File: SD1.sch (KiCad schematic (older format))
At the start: 46 parts, among them J103 JST ZH 1.5mm 1x5, J104 JST 1.25mm, J107 JST 1.25mm, Q101 BSS138, Q102 PDTC114EU,115, SW103 Multidirection_Switch, U102 ER-TFTM028-4, U104 CC2652P, U106 EKMC1691111, U107 MCP23017, U108 BME280, U109 SCD30

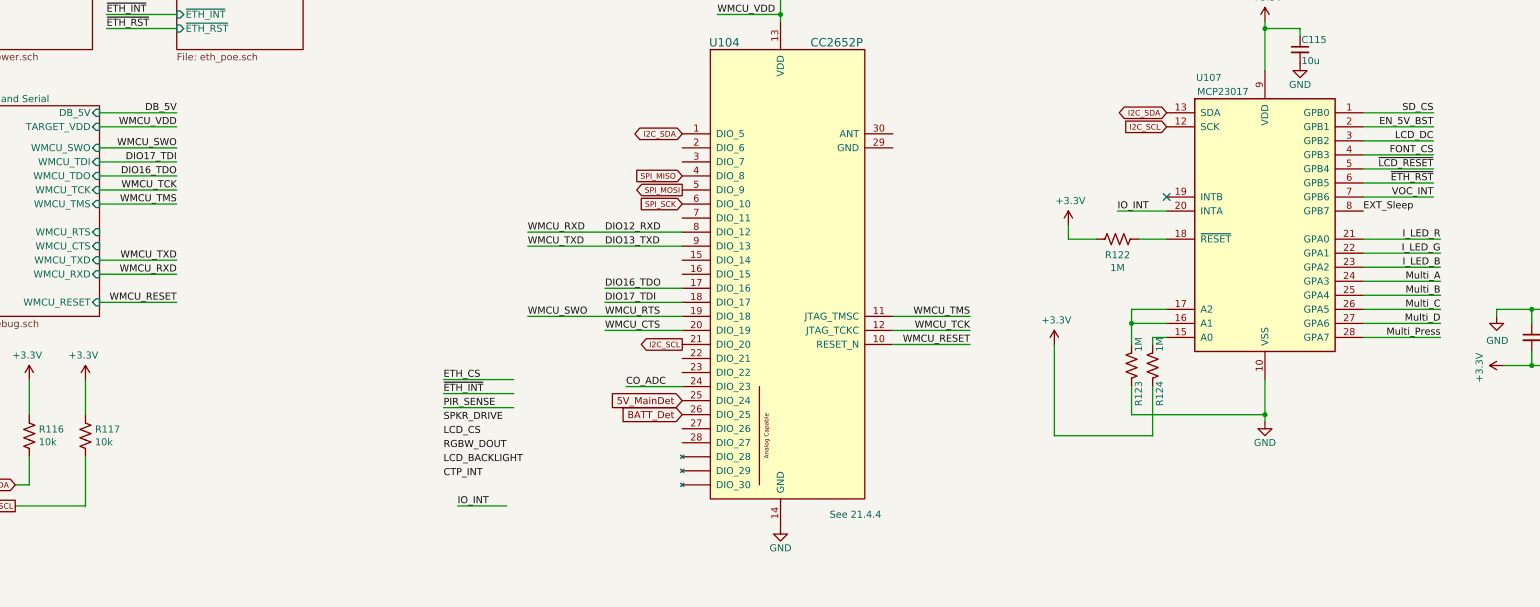
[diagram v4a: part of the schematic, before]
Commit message: 4layer layout WIP, 90%.
Changed SCD30 to reverse mount. 
Connected RGB led and button to io expander.
Connected all nets to micro.
Add jumper for CTS line.
Nettie GNDA and GND for W5500 Eth.
Changed EN_5V_BST to Global.
Bugfixes net names: LCD_CS
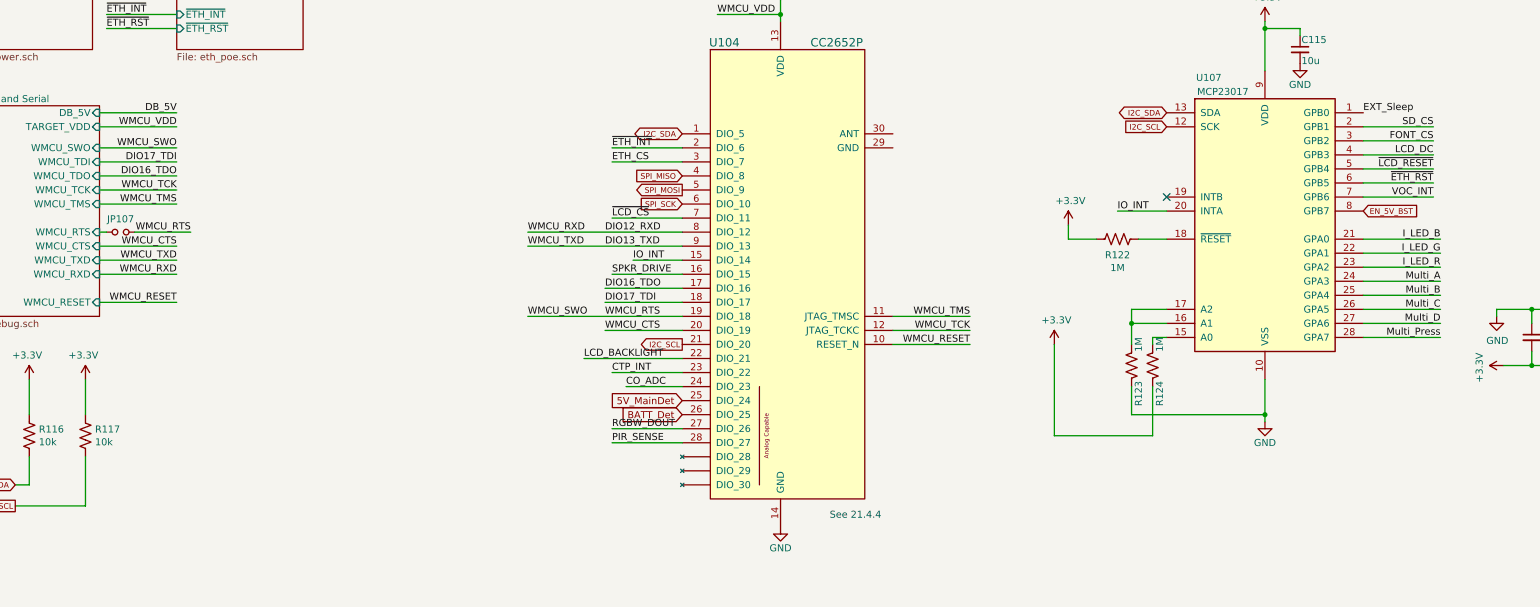
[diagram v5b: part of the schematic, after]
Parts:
- added JP107: Jumper_NO_Small, Jumper:SolderJumper-2_P1.3mm_Open_RoundedPad1.0x1.5mm, symbol Device:Jumper_NO_Small
- U109: footprint mylib:SCD30 -> mylib:SCD30_reverse_mount
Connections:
- net CTP_INT: now also U104.23 (DIO_22)
- net Debug and Serial/WMCU_RTS: now also JP107.1
- net EN_5V_BST: now also U107.8 (GPB7); no longer U107.2 (GPB1)
- net ETH_CS: now also U104.3 (DIO_7)
- net EXT_Sleep: now also U107.1 (GPB0); no longer U107.8 (GPB7)
- net FONT_CS: now also U107.3 (GPB2); no longer U107.4 (GPB3)
- net IO_INT: now also U104.15 (DIO_14)
- net I_LED_B: now also U107.21 (GPA0); no longer U107.23 (GPA2)
- net I_LED_R: now also U107.23 (GPA2); no longer U107.21 (GPA0)
- net LCD_BACKLIGHT: now also U104.22 (DIO_21)
- net LCD_DC: now also U107.4 (GPB3); no longer U107.3 (GPB2)
- net PIR_SENSE: now also U104.28 (DIO_27)
- net RGBW_DOUT: now also U104.27 (DIO_26)
- net SD_CS: now also U107.2 (GPB1); no longer U107.1 (GPB0)
- net SPKR_DRIVE: now also U104.16 (DIO_15)
- net WMCU_RTS: now also JP107.2
- net ~ETH_INT: now also U104.2 (DIO_6)
- net ~LCD_CS: now also U104.7 (DIO_11)
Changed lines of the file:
@@
 Text GLabel 13850 1700 2    40   Output ~ 0
 SPI_MISO
-Text Label 11150 1750 2    50   ~ 0
+Text Label 11150 1850 2    50   ~ 0
 SD_CS
-Text Label 11150 2050 2    50   ~ 0
+Text Label 11150 1950 2    50   ~ 0
 FONT_CS
 Text Label 14050 1050 2    50   ~ 0
 ~LCD_CS
-Text Label 4100 4050 0    50   ~ 0
-LCD_CS
 Text Label 14050 900  2    50   ~ 0
 ~LCD_RESET
@@
 Text Label 14050 1250 2    50   ~ 0
 LCD_DC
-Text Label 11150 1950 2    50   ~ 0
+Text Label 11150 2050 2    50   ~ 0
 LCD_DC
-Text Label 4100 4250 0    50   ~ 0
+Text Label 5100 3500 0    50   ~ 0
 LCD_BACKLIGHT
 Wire Wire Line
@@
 F 0 "U109" H 6097 7671 50  0000 R CNN
 F 1 "SCD30" H 6097 7580 50  0000 R CNN
-F 2 "mylib:SCD30" V 6400 7650 50  0001 C CNN
+F 2 "mylib:SCD30_reverse_mount" V 6400 7650 50  0001 C CNN
 F 3 "https://www.sensirion.com/fileadmin/user_upload/customers/sensirion/Dokumente/9.5_CO2/Sensirion_CO2_Sensors_SCD30_Datasheet.pdf" V 6675 7825 50  0001 C CNN
 F 4 "SCD30" H 6400 7650 50  0001 C CNN "MPN"
@@
 Text GLabel 5800 3800 0    50   Input ~ 0
 5V_MainDet
-Wire Wire Line
-	11150 1850 10650 1850
-Text Label 11150 1850 2    50   ~ 0
-EN_5V_BST
 Text Notes 3700 8800 0    50   ~ 0
 Particulates
@@
 CO_ADC
 Wire Wire Line
-	4100 3850 4600 3850
-Text Label 4100 3850 0    50   ~ 0
+	5300 4100 5800 4100
+Text Label 5300 4100 0    50   ~ 0
 PIR_SENSE
-Text Label 4100 4350 0    50   ~ 0
+Text Label 5300 3600 0    50   ~ 0
 CTP_INT
 Wire Wire Line
@@
 Text Label 11150 2250 2    50   ~ 0
 ~ETH_RST
-Wire Wire Line
-	4100 3750 4600 3750
-Text Label 4100 3750 0    50   ~ 0
-~ETH_INT
-Wire Wire Line
-	4100 3650 4600 3650
-Text Label 4100 3650 0    50   ~ 0
-ETH_CS
-Text Label 4200 4550 0    50   ~ 0
+Text Label 5450 2800 0    50   ~ 0
 IO_INT
 Wire Wire Line
-	4200 4550 4550 4550
+	5450 2800 5800 2800
 Wire Wire Line
 	11150 2350 10650 2350
 Text Label 11150 2350 2    50   ~ 0
 VOC_INT
-Wire Wire Line
-	10650 2650 11200 2650
-Wire Wire Line
-	10650 2750 11200 2750
-Wire Wire Line
-	10650 2850 11200 2850
-Text Label 11200 2650 2    50   ~ 0
-I_LED_R
-Text Label 11200 2750 2    50   ~ 0
-I_LED_G
-Text Label 11200 2850 2    50   ~ 0
-I_LED_B
 NoConn ~ 8550 10150
 Wire Wire Line
@@
 Text Label 8100 9750 0    50   ~ 0
 EXT_Sleep
-Text Label 10650 2450 0    50   ~ 0
+Text Label 10650 1750 0    50   ~ 0
 EXT_Sleep
 Wire Wire Line
@@
 Text Label 11200 3350 2    50   ~ 0
 Multi_Press
-Text Label 4100 3950 0    50   ~ 0
+Text Label 5300 2900 0    50   ~ 0
 SPKR_DRIVE
 Wire Wire Line
 	11150 2150 10650 2150
 Wire Wire Line
-	11150 2050 10650 2050
-Wire Wire Line
 	11150 1950 10650 1950
 $Comp
@@
 $EndComp
 Wire Wire Line
-	11150 1750 10650 1750
+	11150 1850 10650 1850
 Text GLabel 5800 3900 0    50   Input ~ 0
 BATT_Det
@@
 Text Label 14500 7200 0    50   ~ 0
 RGBW_DOUT
-Text Label 4100 4150 0    50   ~ 0
+Text Label 5300 4000 0    50   ~ 0
 RGBW_DOUT
+Text Label 11200 2650 2    50   ~ 0
+I_LED_B
+Text Label 11200 2750 2    50   ~ 0
+I_LED_G
+Text Label 11200 2850 2    50   ~ 0
+I_LED_R
+Wire Wire Line
+	10650 2650 11200 2650
+Wire Wire Line
+	10650 2750 11200 2750
+Wire Wire Line
+	10650 2850 11200 2850
+Wire Wire Line
+	2200 2700 1650 2700
+Text Label 2200 2700 2    50   ~ 0
+WMCU_CTS
+Wire Wire Line
+	1650 2600 1700 2600
+$Comp
+L Device:Jumper_NO_Small JP107
+U 1 1 5FFF492F
+P 1800 2600
+F 0 "JP107" H 1800 2693 50  0000 C CNN
+F 1 "Jumper_NO_Small" H 1800 2694 50  0001 C CNN
+F 2 "Jumper:SolderJumper-2_P1.3mm_Open_RoundedPad1.0x1.5mm" H 1800 2600 50  0001 C CNN
+F 3 "~" H 1800 2600 50  0001 C CNN
+	1    1800 2600
+	1    0    0    -1
+$EndComp
+Text Label 2300 2600 2    50   ~ 0
+WMCU_RTS
+Wire Wire Line
+	2300 2600 1900 2600
+Text GLabel 10650 2450 2    40   Input ~ 0
+EN_5V_BST
+Wire Wire Line
+	10650 2050 11150 2050
+Text Label 5300 2100 0    50   ~ 0
+ETH_CS
+Wire Wire Line
+	5300 2100 5800 2100
+Text Label 5300 2000 0    50   ~ 0
+~ETH_INT
+Wire Wire Line
+	5300 2000 5800 2000
+Wire Wire Line
+	5300 2900 5800 2900
+Wire Wire Line
+	5300 2500 5800 2500
+Text Label 5300 2500 0    50   ~ 0
+~LCD_CS
+Wire Wire Line
+	5300 3600 5800 3600
+Wire Wire Line
+	5300 4000 5800 4000
+Wire Wire Line
+	5100 3500 5800 3500
 $EndSCHEMATC

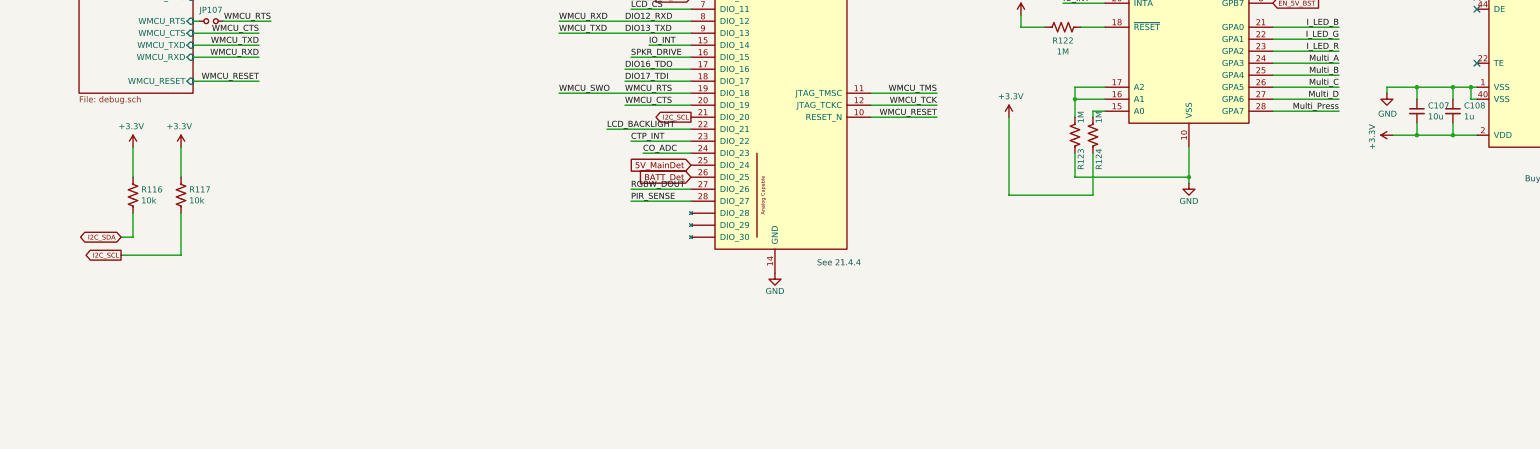
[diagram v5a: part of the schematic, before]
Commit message: Layout WIP, sch final
USB 5V Jumper works for both FTDI and microusb
Added decoupling caps for micro
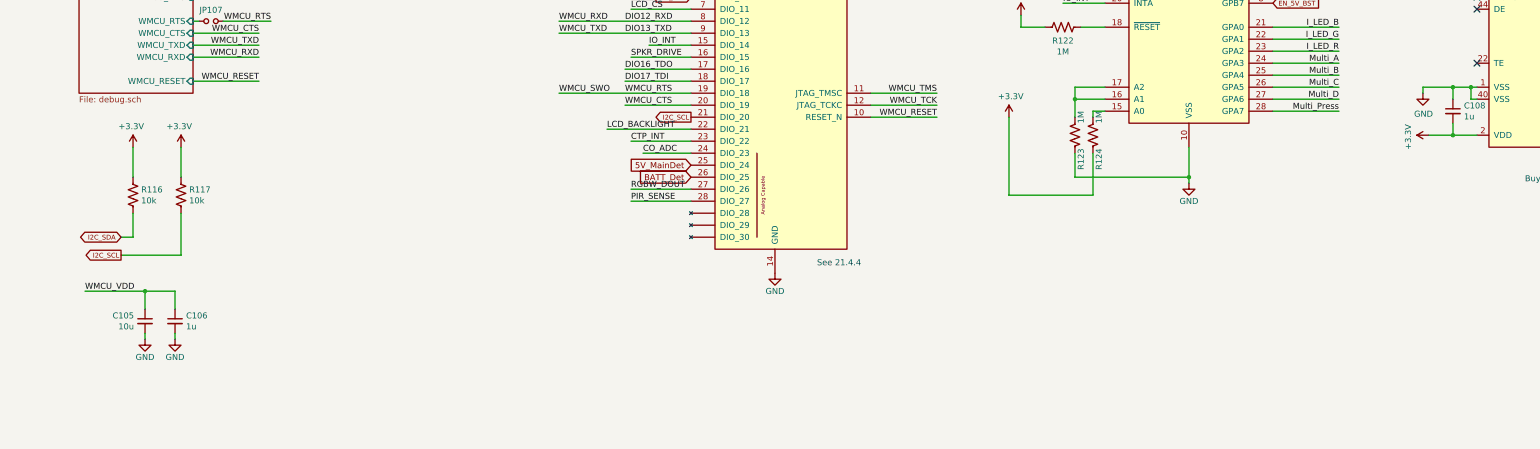
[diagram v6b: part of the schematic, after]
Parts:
- removed C107: 10u, Capacitor_SMD:C_1206_3216Metric, symbol Device:C_Small
- added C105: 10u, Capacitor_SMD:C_0603_1608Metric, symbol Device:C_Small
- added C106: 1u, Capacitor_SMD:C_0603_1608Metric, symbol Device:C_Small
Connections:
- net +3V3: now also C105.1, C106.1
- net GND: now also C105.2, C106.2
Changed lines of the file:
@@
 L power:+3.3V #PWR?
 U 1 1 5FA62239
-P 11650 3550
+P 11950 3550
 AR Path="/5E715318/5FA62239" Ref="#PWR?"  Part="1"
 AR Path="/5FA62239" Ref="#PWR0117"  Part="1"
-F 0 "#PWR0117" H 11650 3400 50  0001 C CNN
-F 1 "+3.3V" H 11665 3723 50  0000 C CNN
-F 2 "" H 11650 3550 50  0001 C CNN
-F 3 "" H 11650 3550 50  0001 C CNN
-	1    11650 3550
+F 0 "#PWR0117" H 11950 3400 50  0001 C CNN
+F 1 "+3.3V" H 11965 3723 50  0000 C CNN
+F 2 "" H 11950 3550 50  0001 C CNN
+F 3 "" H 11950 3550 50  0001 C CNN
+	1    11950 3550
 	0    -1   1    0
 $EndComp
@@
 $Comp
 L Device:C_Small C?
-U 1 1 5FCE922A
-P 11850 3350
-AR Path="/5E360A9B/5FCE922A" Ref="C?"  Part="1"
-AR Path="/5FCE922A" Ref="C107"  Part="1"
-AR Path="/5E5C8043/5E5C885F/5FCE922A" Ref="C?"  Part="1"
-AR Path="/5E5C8043/5E9EE9F0/5FCE922A" Ref="C?"  Part="1"
-AR Path="/5E5C8043/5EA19CBA/5FCE922A" Ref="C?"  Part="1"
-AR Path="/5E5C8043/5E49A000/5FCE922A" Ref="C?"  Part="1"
-AR Path="/5E5C8043/5EAB3002/5FCE922A" Ref="C?"  Part="1"
-AR Path="/5E5C8043/5FCE922A" Ref="C?"  Part="1"
-F 0 "C107" H 11758 3396 50  0000 R CNN
-F 1 "10u" H 11758 3305 50  0000 R CNN
-F 2 "Capacitor_SMD:C_1206_3216Metric" H 11850 3350 50  0001 C CNN
-F 3 "~" H 11850 3350 50  0001 C CNN
-F 4 "CL31A106MAHNNNE" H 11850 3350 50  0001 C CNN "MPN"
-F 5 "1276-1181-1-ND" H 11850 3350 50  0001 C CNN "Digikey"
-F 6 "CAP CER 10UF 25V X5R 1206" H 11850 3350 50  0001 C CNN "Note"
-	1    11850 3350
-	-1   0    0    -1
-$EndComp
-$Comp
-L Device:C_Small C?
 U 1 1 5FCE9233
 P 12150 3350
@@
 Wire Wire Line
 	12150 3150 12300 3150
-Wire Wire Line
-	12150 3150 11850 3150
 Connection ~ 12150 3150
 Wire Wire Line
-	11850 3450 11850 3550
-Connection ~ 11850 3550
-Wire Wire Line
-	11850 3550 12150 3550
-Wire Wire Line
 	12300 3250 12300 3150
 Wire Wire Line
@@
 	12150 3150 12150 3250
 Wire Wire Line
-	11850 3150 11850 3250
-Wire Wire Line
-	11850 3150 11600 3150
-Wire Wire Line
-	11600 3150 11600 3200
-Connection ~ 11850 3150
+	11900 3150 11900 3200
 $Comp
 L power:GND #PWR0114
 U 1 1 5FDF9CCC
-P 11600 3200
-F 0 "#PWR0114" H 11600 2950 50  0001 C CNN
-F 1 "GND" H 11605 3027 50  0000 C CNN
-F 2 "" H 11600 3200 50  0001 C CNN
-F 3 "" H 11600 3200 50  0001 C CNN
-	1    11600 3200
+P 11900 3200
+F 0 "#PWR0114" H 11900 2950 50  0001 C CNN
+F 1 "GND" H 11905 3027 50  0000 C CNN
+F 2 "" H 11900 3200 50  0001 C CNN
+F 3 "" H 11900 3200 50  0001 C CNN
+	1    11900 3200
 	1    0    0    -1
 $EndComp
-Wire Wire Line
-	11650 3550 11850 3550
 $Bitmap
 Pos 19450 2500
@@
 Wire Wire Line
 	5100 3500 5800 3500
+Wire Wire Line
+	11900 3150 12150 3150
+Wire Wire Line
+	11950 3550 12150 3550
+$Comp
+L Device:C_Small C105
+U 1 1 5FD80450
+P 1250 5100
+F 0 "C105" H 1158 5146 50  0000 R CNN
+F 1 "10u" H 1158 5055 50  0000 R CNN
+F 2 "Capacitor_SMD:C_0603_1608Metric" H 1250 5100 50  0001 C CNN
+F 3 "" H 1250 5100 50  0001 C CNN
+F 4 "445-6853-1-ND" H 1250 5100 50  0001 C CNN "Digikey"
+F 5 "C1608X5R1A106M080AC" H 1250 5100 50  0001 C CNN "MPN"
+F 6 "CAP CER 10UF 10V X5R 0603" H 1250 5100 50  0001 C CNN "Note"
+	1    1250 5100
+	1    0    0    -1
+$EndComp
+$Comp
+L Device:C_Small C?
+U 1 1 5FD84CCD
+P 1500 5100
+AR Path="/5E360A9B/5FD84CCD" Ref="C?"  Part="1"
+AR Path="/5FD84CCD" Ref="C106"  Part="1"
+AR Path="/5E5C8043/5E5C885F/5FD84CCD" Ref="C?"  Part="1"
+AR Path="/5E5C8043/5E9EE9F0/5FD84CCD" Ref="C?"  Part="1"
+AR Path="/5E5C8043/5EA19CBA/5FD84CCD" Ref="C?"  Part="1"
+AR Path="/5E5C8043/5E49A000/5FD84CCD" Ref="C?"  Part="1"
+AR Path="/5E5C8043/5EAB3002/5FD84CCD" Ref="C?"  Part="1"
+AR Path="/5E5C8043/5FD84CCD" Ref="C?"  Part="1"
+F 0 "C106" H 1408 5146 50  0000 R CNN
+F 1 "1u" H 1408 5055 50  0000 R CNN
+F 2 "Capacitor_SMD:C_0603_1608Metric" H 1500 5100 50  0001 C CNN
+F 3 "~" H 1500 5100 50  0001 C CNN
+F 4 "TMK107B7105KA-T" H 1500 5100 50  0001 C CNN "MPN"
+F 5 "587-2984-1-ND" H 1500 5100 50  0001 C CNN "Digikey"
+F 6 "CAP CER 1UF 25V X7R 0603" H 1500 5100 50  0001 C CNN "Note"
+	1    1500 5100
+	-1   0    0    -1
+$EndComp
+Text Label 750  4850 0    50   ~ 0
+WMCU_VDD
+Wire Wire Line
+	1250 4850 1250 5000
+Wire Wire Line
+	750  4850 1250 4850
+Wire Wire Line
+	1250 4850 1500 4850
+Wire Wire Line
+	1500 4850 1500 5000
+Connection ~ 1250 4850
+$Comp
+L power:GND #PWR0211
+U 1 1 5FDB9EFA
+P 1500 5250
+F 0 "#PWR0211" H 1500 5000 50  0001 C CNN
+F 1 "GND" H 1500 5100 50  0000 C CNN
+F 2 "" H 1500 5250 50  0001 C CNN
+F 3 "" H 1500 5250 50  0001 C CNN
+	1    1500 5250
+	-1   0    0    -1
+$EndComp
+$Comp
+L power:GND #PWR0212
+U 1 1 5FDBA34D
+P 1250 5250
+F 0 "#PWR0212" H 1250 5000 50  0001 C CNN
+F 1 "GND" H 1250 5100 50  0000 C CNN
+F 2 "" H 1250 5250 50  0001 C CNN
+F 3 "" H 1250 5250 50  0001 C CNN
+	1    1250 5250
+	-1   0    0    -1
+$EndComp
+Wire Wire Line
+	1250 5250 1250 5200
+Wire Wire Line
+	1500 5250 1500 5200
 $EndSCHEMATC

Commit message: Re-annotate all parts
Cleans up annotations
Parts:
- renumbered C115 to C101, C108 to C102, C105 to C103, C106 to C104, C110 to C105, C112 to C106, C114 to C107, C109 to C108, D105 to D101, FB102 to FB101, J104 to J101, J107 to J102, JP107 to JP103, JP103 to JP104, R118 to R101, R122 to R102, R123 to R103, R124 to R104, R116 to R105, R117 to R106, R114 to R107, R115 to R108, R108 to R109, R111 to R110, R112 to R111, R113 to R112, R109 to R113, R110 to R114, R107 to R115, SW103 to SW101, U102 to U101, U107 to U102, U104 to U103, U109 to U104, U108 to U105

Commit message: Prefinal, layout done
Update FB to use inductor footprints
DNP net tie
Update diode symbol in power
Add battery voltage divider in power
Supply 5V power to aux sensor connector
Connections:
- net +5V: now also J102.1 (VDD)
- no-connect marks 32 -> 31
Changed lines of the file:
@@
 	-1   0    0    -1
 $EndComp
-NoConn ~ 8550 9550
 NoConn ~ 8550 10050
 NoConn ~ 8550 10250
-$Comp
-L mylib:RECAPS_Master_r0 J?
-U 1 1 5FAEBA7D
-P 8850 9800
-AR Path="/5B315020/5FAEBA7D" Ref="J?"  Part="1"
-AR Path="/5E7F0E36/5FAEBA7D" Ref="J?"  Part="1"
-AR Path="/5EAEE4A6/5FAEBA7D" Ref="J?"  Part="1"
-AR Path="/5EBCC09F/5FAEBA7D" Ref="J?"  Part="1"
-AR Path="/5EBCC0E4/5FAEBA7D" Ref="J?"  Part="1"
-AR Path="/5F039000/5FAEBA7D" Ref="J?"  Part="1"
-AR Path="/5F039043/5FAEBA7D" Ref="J?"  Part="1"
-AR Path="/5FE46632/5FAEBA7D" Ref="J?"  Part="1"
-AR Path="/5FE6596A/5FAEBA7D" Ref="J?"  Part="1"
-AR Path="/5FAEBA7D" Ref="J102"  Part="1"
-F 0 "J102" H 8768 9175 50  0000 C CNN
-F 1 "JST 1.25mm" H 8768 9266 50  0000 C CNN
-F 2 "Connector_Molex:Molex_PicoBlade_53398-0871_1x08-1MP_P1.25mm_Vertical" H 8850 9800 50  0001 C CNN
-F 3 "" H 8850 9800 50  0001 C CNN
-F 4 "0533980871" H 8850 9800 50  0001 C CNN "MPN"
-F 5 "-" H 8850 9800 50  0001 C CNN "Mouser"
-F 6 "WM7612CT-ND" H 8850 9800 50  0001 C CNN "Digikey"
-	1    8850 9800
-	-1   0    0    -1
-$EndComp
 Text Notes 16900 4400 0    50   ~ 0
 See: https://www.buydisplay.com/download/interfacing/ER-TFTM028-4_Interfacing.pdf
@@
 Wire Wire Line
 	1500 5250 1500 5200
+$Comp
+L mylib:RECAPS_Master_r0 J?
+U 1 1 5FAEBA7D
+P 8850 9800
+AR Path="/5B315020/5FAEBA7D" Ref="J?"  Part="1"
+AR Path="/5E7F0E36/5FAEBA7D" Ref="J?"  Part="1"
+AR Path="/5EAEE4A6/5FAEBA7D" Ref="J?"  Part="1"
+AR Path="/5EBCC09F/5FAEBA7D" Ref="J?"  Part="1"
+AR Path="/5EBCC0E4/5FAEBA7D" Ref="J?"  Part="1"
+AR Path="/5F039000/5FAEBA7D" Ref="J?"  Part="1"
+AR Path="/5F039043/5FAEBA7D" Ref="J?"  Part="1"
+AR Path="/5FE46632/5FAEBA7D" Ref="J?"  Part="1"
+AR Path="/5FE6596A/5FAEBA7D" Ref="J?"  Part="1"
+AR Path="/5FAEBA7D" Ref="J102"  Part="1"
+F 0 "J102" H 8768 9175 50  0000 C CNN
+F 1 "JST 1.25mm" H 8768 9266 50  0000 C CNN
+F 2 "Connector_Molex:Molex_PicoBlade_53398-0871_1x08-1MP_P1.25mm_Vertical" H 8850 9800 50  0001 C CNN
+F 3 "" H 8850 9800 50  0001 C CNN
+F 4 "0533980871" H 8850 9800 50  0001 C CNN "MPN"
+F 5 "-" H 8850 9800 50  0001 C CNN "Mouser"
+F 6 "WM7612CT-ND" H 8850 9800 50  0001 C CNN "Digikey"
+	1    8850 9800
+	-1   0    0    -1
+$EndComp
+Wire Wire Line
+	8450 9550 8550 9550
+Wire Wire Line
+	8450 9450 8450 9550
+$Comp
+L power:+5V #PWR0144
+U 1 1 5FD50347
+P 8450 9450
+F 0 "#PWR0144" H 8450 9300 50  0001 C CNN
+F 1 "+5V" H 8465 9623 50  0000 C CNN
+F 2 "" H 8450 9450 50  0001 C CNN
+F 3 "" H 8450 9450 50  0001 C CNN
+	1    8450 9450
+	-1   0    0    -1
+$EndComp
 $EndSCHEMATC
